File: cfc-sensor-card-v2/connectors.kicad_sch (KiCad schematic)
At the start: 4 parts, among them J1 J-SAMTEC-TFM-120-01-L-D-RA, J3 J-SAMTEC-TFM-110-01-L-D-RA

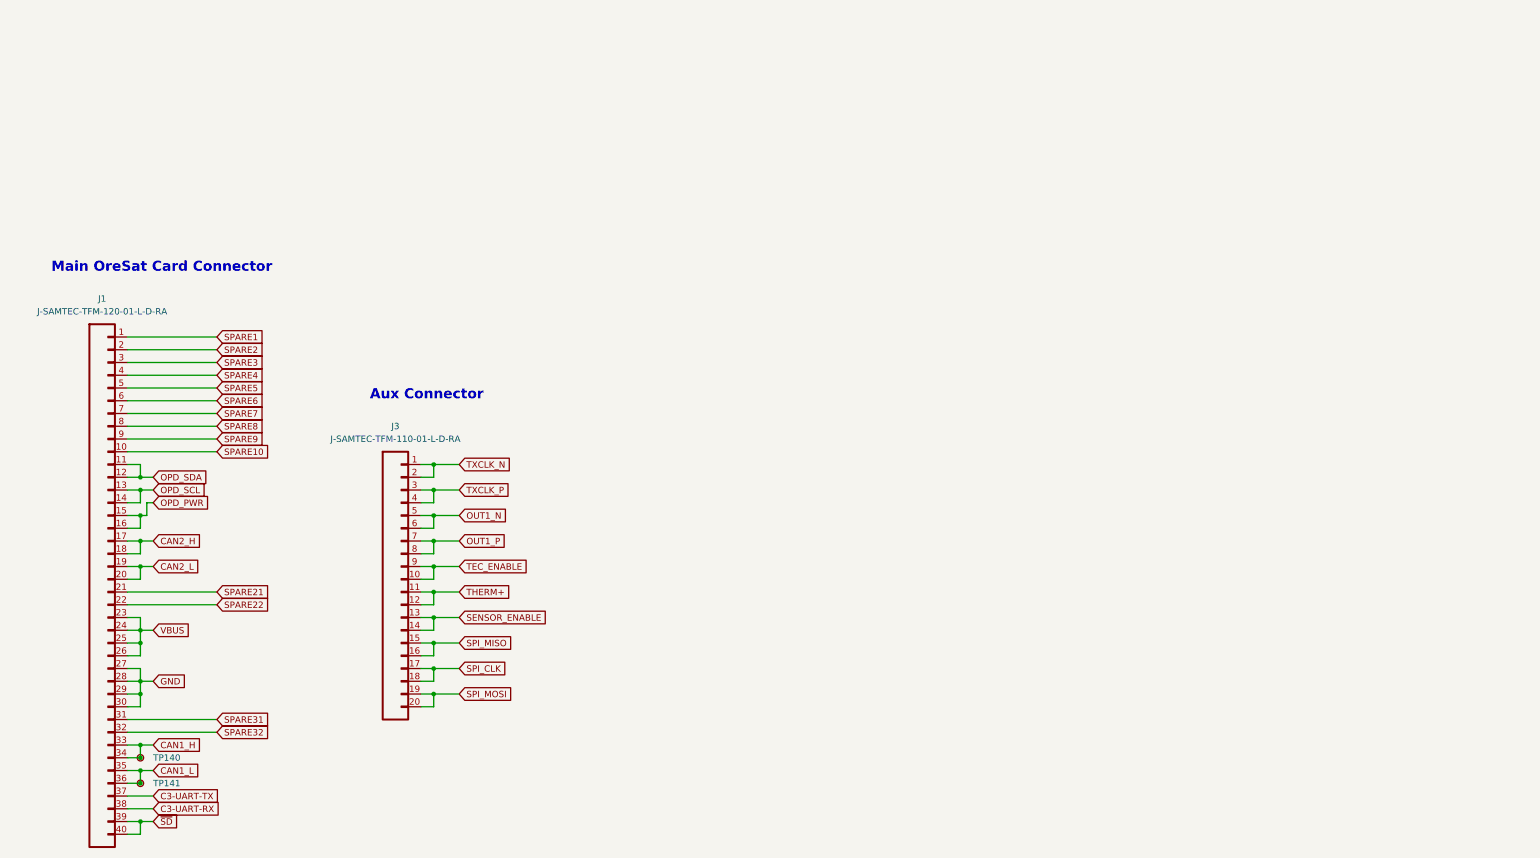
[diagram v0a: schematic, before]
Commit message: Big sweep through to clean up from v2.0 to v2.1 board. Cleaned up all of the Github issues, and even added a MPS2410A CC driver to run the TEC for increased efficiency. Left old switch on board just in case. Lots of cleanup, added some documentation, added pin holes for 1.5 mm alignment pins, now version 2.1
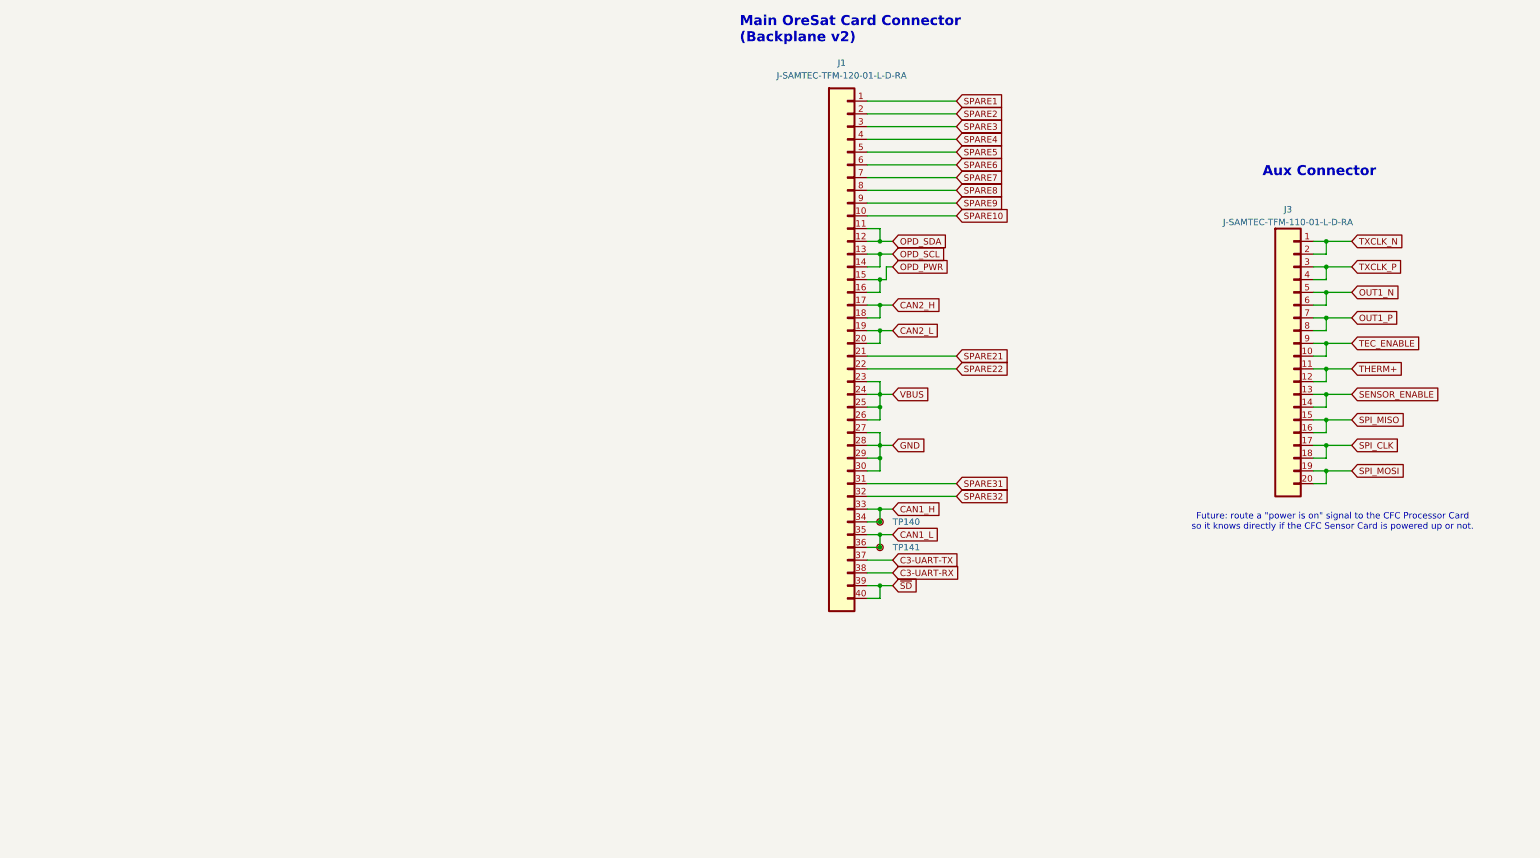
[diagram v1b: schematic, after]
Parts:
- J3: DIST Digikey -> (none); DPN SAM10113-ND -> (none); MFR SAMTEC -> (none); MPN TFM-110-01-L-D-RA -> (none)
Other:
- note added: "Future: route a "power is on" signal to the CFC Processor Card so it knows directly if the CFC Sensor Card is powered up or not."
- note added: "Main OreSat Card Connector (Backplane v2)"
- note removed: "Main OreSat Card Connector"
- company: (none) -> Portland State Aerospace Society
- title: (none) -> CFC Sensor Card
- moved on the sheet: TP140, TP141
